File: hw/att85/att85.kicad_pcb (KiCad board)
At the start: 4 copper layers, 80 x 40 mm, 45 parts, among them J101 Barrel_Jack_Switch, J102 Screw_Terminal_01x03, J201 Conn_01x06, Q101 BC817, SW401 SW_Push, SW402 SW_Push, SW403 SW_Push, SW404 SW_Push, SW405 SW_Push, SW406 SW_Push, U201 STM32G030K8Tx, U202 74AHCT125, U301 VS1838B, U401 4050, U501 AMS1117-3.3

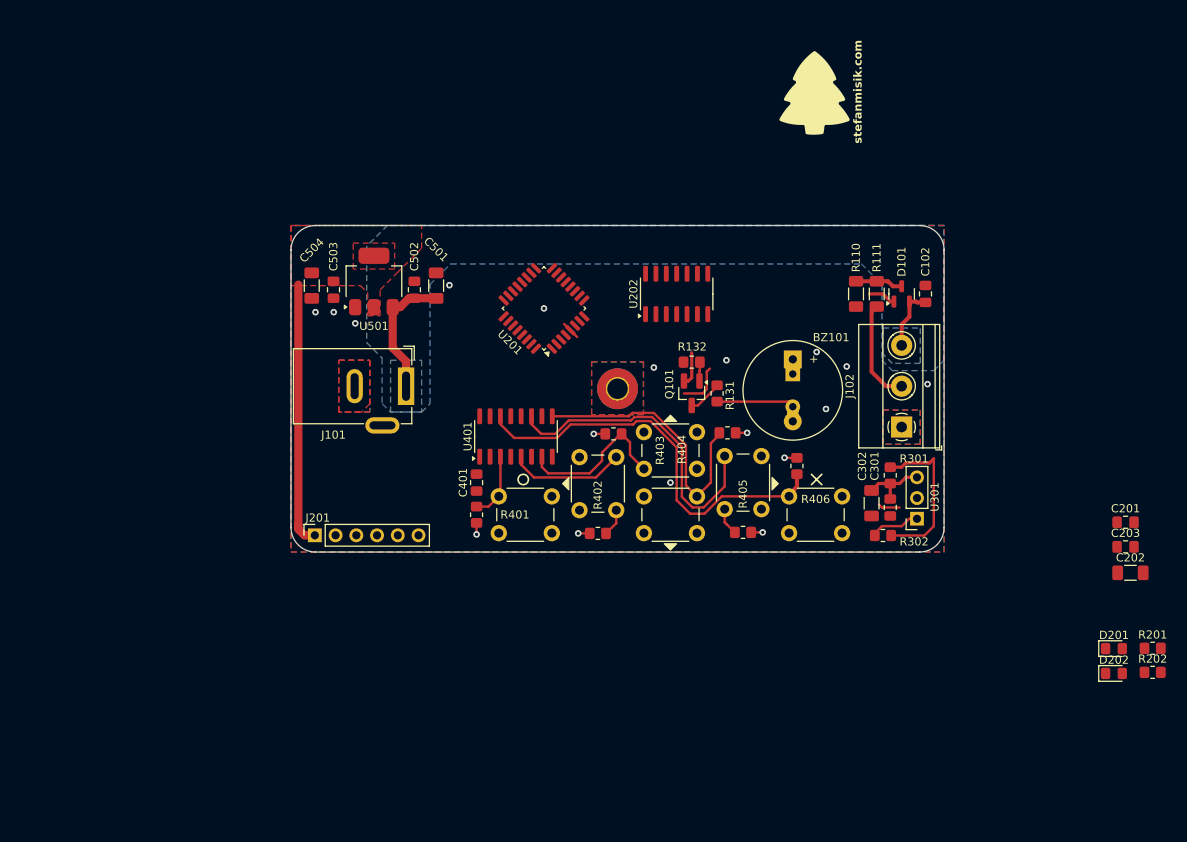
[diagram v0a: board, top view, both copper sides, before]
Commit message: chore(hw): add peripheral connections, layout power supply
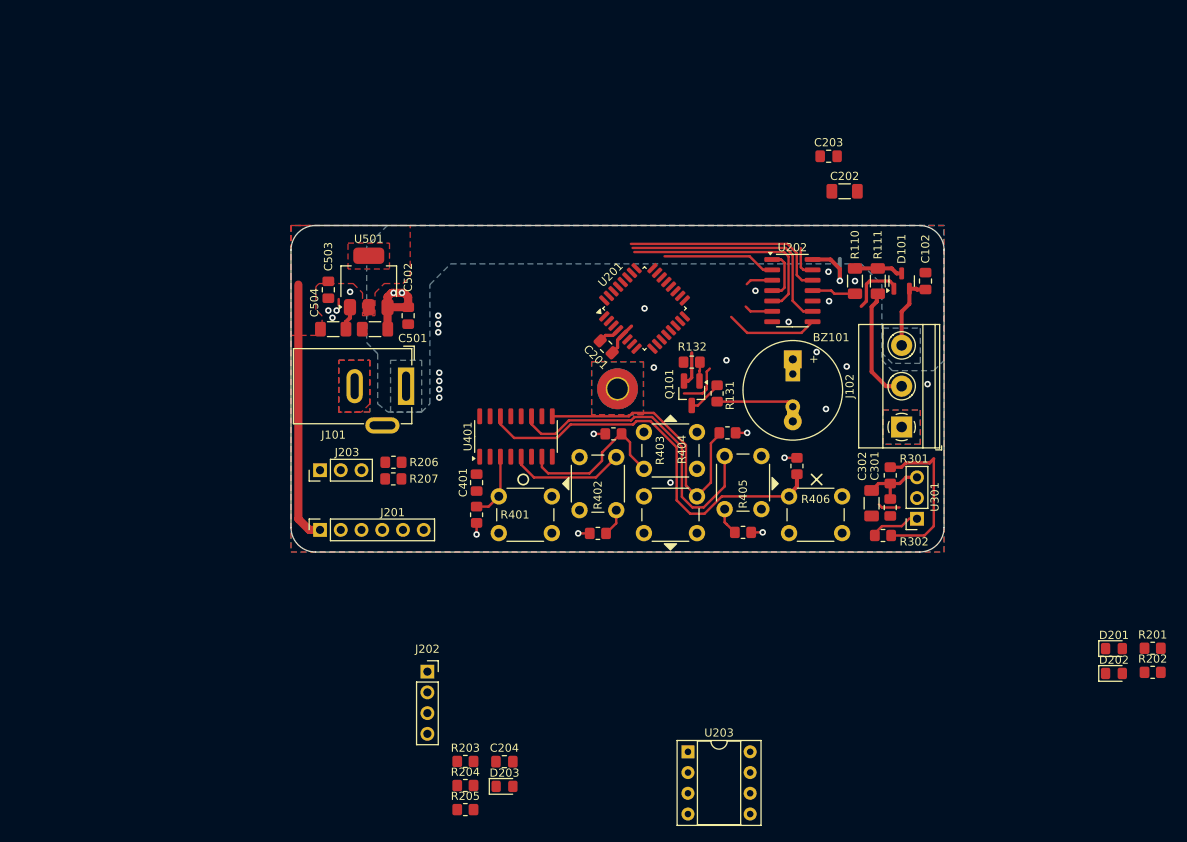
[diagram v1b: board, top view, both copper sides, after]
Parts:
- added C204: 100n, Capacitor_SMD:C_0805_2012Metric_Pad1.18x1.45mm_HandSolder, F.Cu at (145.5, 140.6)
- added D203: LED, LED_SMD:LED_0805_2012Metric_Pad1.15x1.40mm_HandSolder, F.Cu at (145.5, 143.6)
- added J202: Conn_01x04, Connector_PinSocket_2.54mm:PinSocket_1x04_P2.54mm_Vertical, F.Cu at (136.1, 129.6)
- added J203: Conn_01x03, Connector_PinHeader_2.54mm:PinHeader_1x03_P2.54mm_Vertical, F.Cu at (122.9, 104.9)
- added R203: 1K, Resistor_SMD:R_0805_2012Metric_Pad1.20x1.40mm_HandSolder, F.Cu at (140.7, 140.6)
- added R204: 10K, Resistor_SMD:R_0805_2012Metric_Pad1.20x1.40mm_HandSolder, F.Cu at (140.7, 143.5)
- added R205: 10K, Resistor_SMD:R_0805_2012Metric_Pad1.20x1.40mm_HandSolder, F.Cu at (140.7, 146.5)
- added R206: 33R, Resistor_SMD:R_0805_2012Metric_Pad1.20x1.40mm_HandSolder, F.Cu at (131.9, 103.9)
- added R207: 33R, Resistor_SMD:R_0805_2012Metric_Pad1.20x1.40mm_HandSolder, F.Cu at (131.9, 106.0)
- added U203: CAT24C256, Package_DIP:DIP-8_W7.62mm_Socket, F.Cu at (168.0, 139.4)
- moved C201 67.2 mm to (158.0, 89.8), turned to -45 degrees
- moved C203 60.1 mm to (185.2, 66.4)
- moved C202 58.4 mm to (187.2, 70.7)
- moved U202 14.2 mm to (180.8, 82.9), turned to 0 degrees
- moved U201 12.3 mm to (162.7, 85.1), turned to 45 degrees
- moved C501 9.20 mm to (129.7, 87.6), turned to 180 degrees
- moved C504 5.95 mm to (124.5, 87.6), turned to 0 degrees
- moved C502 3.27 mm to (133.7, 86.0), turned to -90 degrees
- moved R110 1.58 mm to (188.5, 81.7)
- moved R111 1.58 mm to (191.3, 81.7)
- moved C102 1.57 mm to (197.1, 81.7)
- moved D101 1.57 mm to (194.2, 81.7)
- moved J201 0.92 mm to (122.9, 112.2)
- moved C503 0.64 mm to (124.0, 82.8)
- moved U501 0.63 mm to (128.9, 81.8)
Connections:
- U201 pad 1: unconnected-(U201-PB9-Pad1) -> /CPU/I2C_SDA
- U201 pad 10: unconnected-(U201-PA3-Pad10) -> /CPU/DEBUG_RX
- U201 pad 16: unconnected-(U201-PB1-Pad16) -> /CPU/STATUS_LED1
- U201 pad 17: unconnected-(U201-PB2-Pad17) -> /CPU/STATUS_LED2
- U201 pad 18: unconnected-(U201-PA8-Pad18) -> /CPU/STATUS_LED3
- U201 pad 32: unconnected-(U201-PB8-Pad32) -> /CPU/I2C_SCL
- U201 pad 9: unconnected-(U201-PA2-Pad9) -> /CPU/DEBUG_TX
- U202 pad 11: unconnected-(U202-Pad11) -> /CPU/LED_DATA
- U202 pad 12: GND -> /CPU/LED_DATA_3V3
- U202 pad 2: /CPU/LED_DATA_3V3 -> /CPU/STATUS_LED1
- U202 pad 3: /CPU/LED_DATA -> Net-(D201-A)
- U202 pad 5: /CPU/STATUS_LED_G -> /CPU/STATUS_LED2
- U202 pad 6: Net-(D201-A) -> Net-(D202-A)
- U202 pad 8: Net-(D202-A) -> Net-(D203-A)
- U202 pad 9: /CPU/STATUS_LED_R -> /CPU/STATUS_LED3
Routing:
- net /CPU/STATUS_LED3: track 0.00 -> 28.6 mm
- net /CPU/STATUS_LED2: track 0.00 -> 26.1 mm
- net /CPU/LED_DATA_3V3: track 0.00 -> 25.7 mm
- net GND: track 18.2 -> 38.0 mm, vias 12 -> 24
- net /CPU/STATUS_LED1: track 0.00 -> 13.9 mm
- net Net-(D203-A): track 0.00 -> 11.3 mm
- net /CPU/LED_DATA: track 0.00 -> 5.48 mm
- net +5V: track 102.3 -> 106.4 mm, vias 6 -> 9
- net Net-(D202-A): track 0.00 -> 3.48 mm
- net Net-(D201-A): track 0.00 -> 3.31 mm
- net +3.3V: track 52.0 -> 54.4 mm
- net Net-(J102-Pin_2): track 12.7 -> 14.2 mm

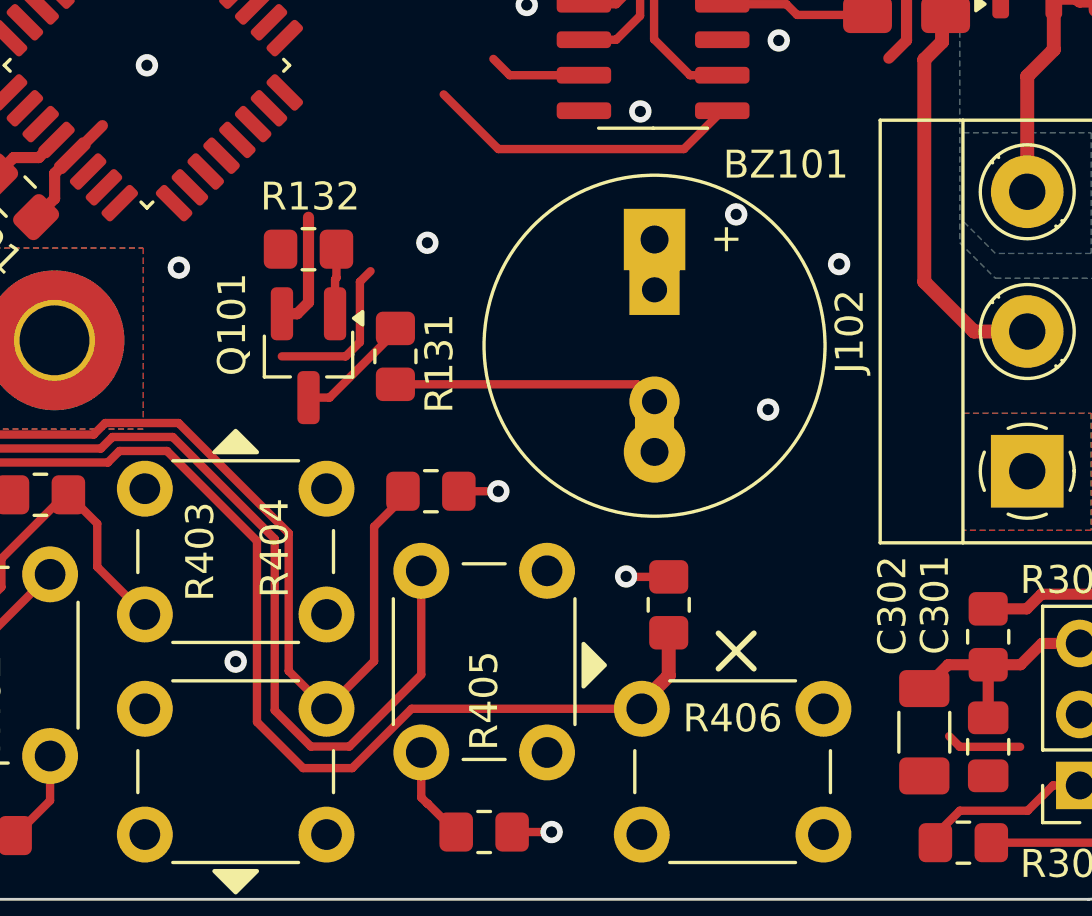
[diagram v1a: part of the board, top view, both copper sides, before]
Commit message: chore(hw): move buzzer driving circuitry
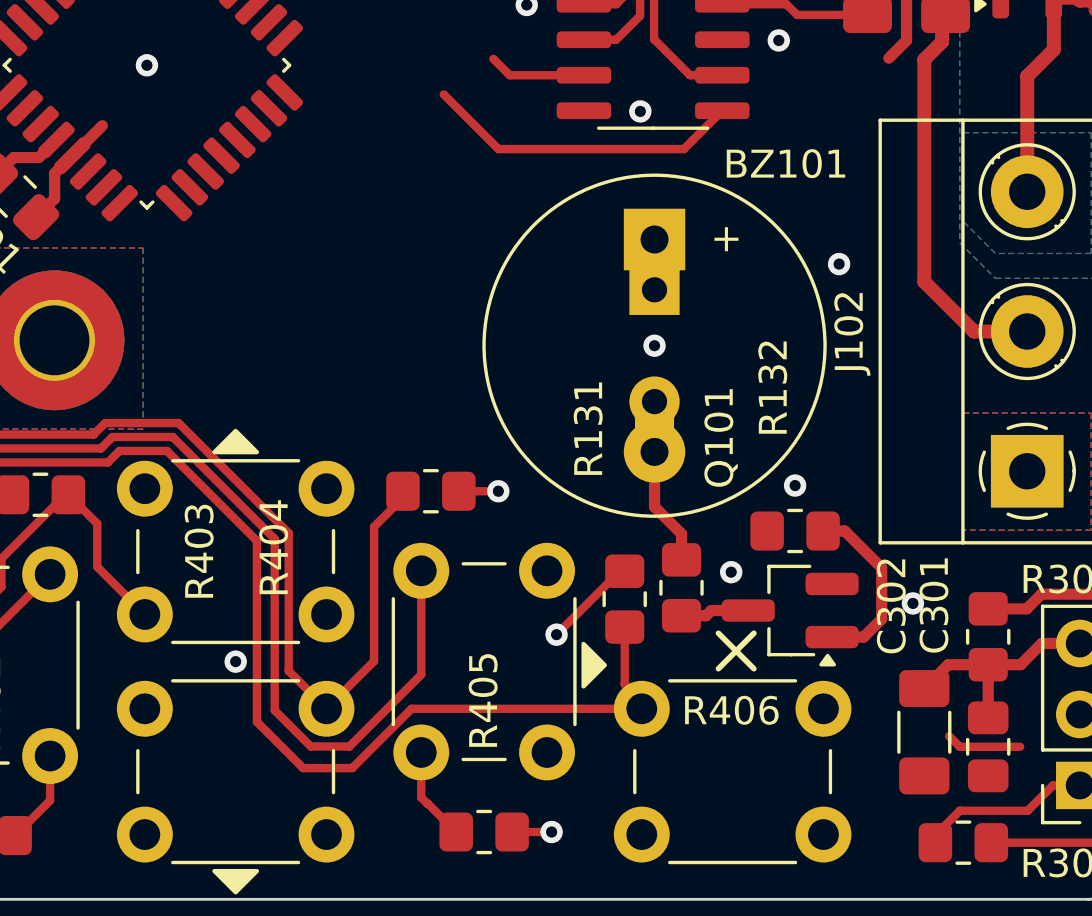
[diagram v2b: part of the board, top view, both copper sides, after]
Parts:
- moved R132 20.1 mm to (185.9, 101.8)
- moved Q101 19.5 mm to (185.7, 104.6), turned to 180 degrees
- moved R131 13.2 mm to (181.8, 103.8), turned to -90 degrees
- moved R406 1.59 mm to (179.8, 104.2)
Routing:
- net GND: track 38.0 -> 28.1 mm
- net Net-(BZ101--): track 9.53 -> 4.26 mm
- net Net-(Q101-B): track 2.33 -> 6.52 mm
- net +5V: track 106.4 -> 104.5 mm
- net Net-(Q101-C): track 4.20 -> 2.47 mm

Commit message: chore(hw): prepare layout
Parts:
- moved J202 93.3 mm to (215.3, 80.3), turned to 90 degrees
- moved U203 86.4 mm to (87.1, 109.0)
- moved C202 13.4 mm to (185.9, 84.1), turned to -90 degrees
- moved C203 13.1 mm to (185.8, 79.5), turned to 90 degrees
- moved U201 10.4 mm to (152.3, 85.0)
- moved C201 10.4 mm to (147.6, 89.7)
- moved C102 3.30 mm to (196.0, 84.8), turned to 180 degrees
- moved C401 2.62 mm to (144.5, 105.4), turned to 0 degrees
- moved J201 2.11 mm to (122.9, 110.1)
- moved R402 1.78 mm to (158.8, 112.5)
- moved R405 1.78 mm to (173.0, 112.5)
- moved D101 1.65 mm to (195.8, 81.7)
- moved R110 1.65 mm to (190.1, 81.7)
- moved R111 1.65 mm to (192.9, 81.7)
- moved U401 0.66 mm to (147.6, 100.6)
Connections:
- U401 pad 10: /CPU/BTN_DOWN -> /CPU/BTN_UP
- U401 pad 11: Net-(R405-Pad1) -> Net-(R406-Pad1)
- U401 pad 12: /CPU/BTN_RIGHT -> /CPU/BTN_X
- U401 pad 14: Net-(R406-Pad1) -> Net-(R405-Pad1)
- U401 pad 15: /CPU/BTN_X -> /CPU/BTN_RIGHT
- U401 pad 6: /CPU/BTN_UP -> /CPU/BTN_DOWN
- U401 pad 7: Net-(R403-Pad1) -> Net-(R404-Pad1)
- U401 pad 9: Net-(R404-Pad1) -> Net-(R403-Pad1)
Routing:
- net +3.3V: track 54.4 -> 139.8 mm, vias 0 -> 2
- net GND: track 28.1 -> 100.9 mm, vias 24 -> 26
- net +5V: track 104.5 -> 151.4 mm
- net /CPU/IR_DATA_3V3: track 6.17 -> 32.4 mm
- net /CPU/BTN_DOWN: track 0.00 -> 13.2 mm
- net /CPU/BTN_LEFT: track 0.00 -> 11.2 mm
- net Net-(R404-Pad1): track 40.4 -> 29.9 mm
- net /CPU/BUZZER_3V3: track 0.00 -> 10.1 mm
- net /CPU/BTN_O: track 0.00 -> 9.41 mm
- net Net-(R406-Pad1): track 56.9 -> 48.8 mm
- net Net-(R405-Pad1): track 48.8 -> 43.5 mm
- net Net-(R403-Pad1): track 25.9 -> 21.5 mm
- net /CPU/BTN_X: track 0.00 -> 2.60 mm
- net /CPU/BTN_RIGHT: track 0.00 -> 2.48 mm
- net /CPU/BTN_UP: track 0.00 -> 2.35 mm
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
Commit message: chore(hw): add buzzer connection
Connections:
- U201 pad 13: unconnected-(U201-PA6-Pad13) -> /CPU/BUZZER_3V3

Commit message: chore(hw): partial layout
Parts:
- moved U203 125.9 mm to (213.0, 104.9)
- moved R202 72.6 mm to (168.9, 83.4), turned to 180 degrees
- moved R201 72.1 mm to (168.9, 81.3), turned to 180 degrees
- moved D202 66.4 mm to (172.7, 83.4)
- moved D201 65.7 mm to (172.7, 81.3)
- moved D203 64.1 mm to (172.7, 85.6)
- moved R203 61.8 mm to (168.9, 85.6), turned to 180 degrees
- moved C201 16.7 mm to (164.2, 90.9), turned to 90 degrees
- moved U201 7.12 mm to (159.4, 85.2), turned to 90 degrees
- moved R207 3.10 mm to (132.0, 102.9)
- moved R132 1.76 mm to (187.2, 100.6), turned to -90 degrees
- moved R206 0.97 mm to (132.0, 104.9)
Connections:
- U201 pad 26: unconnected-(U201-PA15-Pad26) -> /CPU/BTN_O
- U201 pad 27: unconnected-(U201-PB3-Pad27) -> /CPU/BTN_LEFT
- U201 pad 28: unconnected-(U201-PB4-Pad28) -> /CPU/BTN_DOWN
- U201 pad 29: unconnected-(U201-PB5-Pad29) -> /CPU/BTN_RIGHT
- U201 pad 30: unconnected-(U201-PB6-Pad30) -> /CPU/BTN_X
- U201 pad 31: unconnected-(U201-PB7-Pad31) -> /CPU/BTN_UP
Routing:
- net GND: track 100.9 -> 227.7 mm, vias 26 -> 34
- net /CPU/SWDIO: track 0.00 -> 55.8 mm, vias 0 -> 1
- net /CPU/DEBUG_TX: track 0.00 -> 55.6 mm, vias 0 -> 2
- net /CPU/DEBUG_RX: track 0.00 -> 54.5 mm, vias 0 -> 2
- net /CPU/SWCLK: track 0.00 -> 53.9 mm, vias 0 -> 1
- net /CPU/~{RESET}: track 0.00 -> 51.4 mm, vias 0 -> 1
- net +3.3V: track 139.8 -> 178.9 mm, vias 2 -> 4
- net /CPU/IR_DATA_3V3: track 32.4 -> 66.7 mm, vias 0 -> 2
- net /CPU/BUZZER_3V3: track 10.1 -> 35.4 mm
- net /CPU/BTN_O: track 9.41 -> 32.5 mm
- net /CPU/BTN_LEFT: track 11.2 -> 33.2 mm
- net /CPU/BTN_DOWN: track 13.2 -> 34.3 mm
- net /CPU/BTN_RIGHT: track 2.48 -> 20.6 mm
- net /CPU/BTN_X: track 2.60 -> 16.8 mm
- net +5V: track 151.4 -> 163.6 mm
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
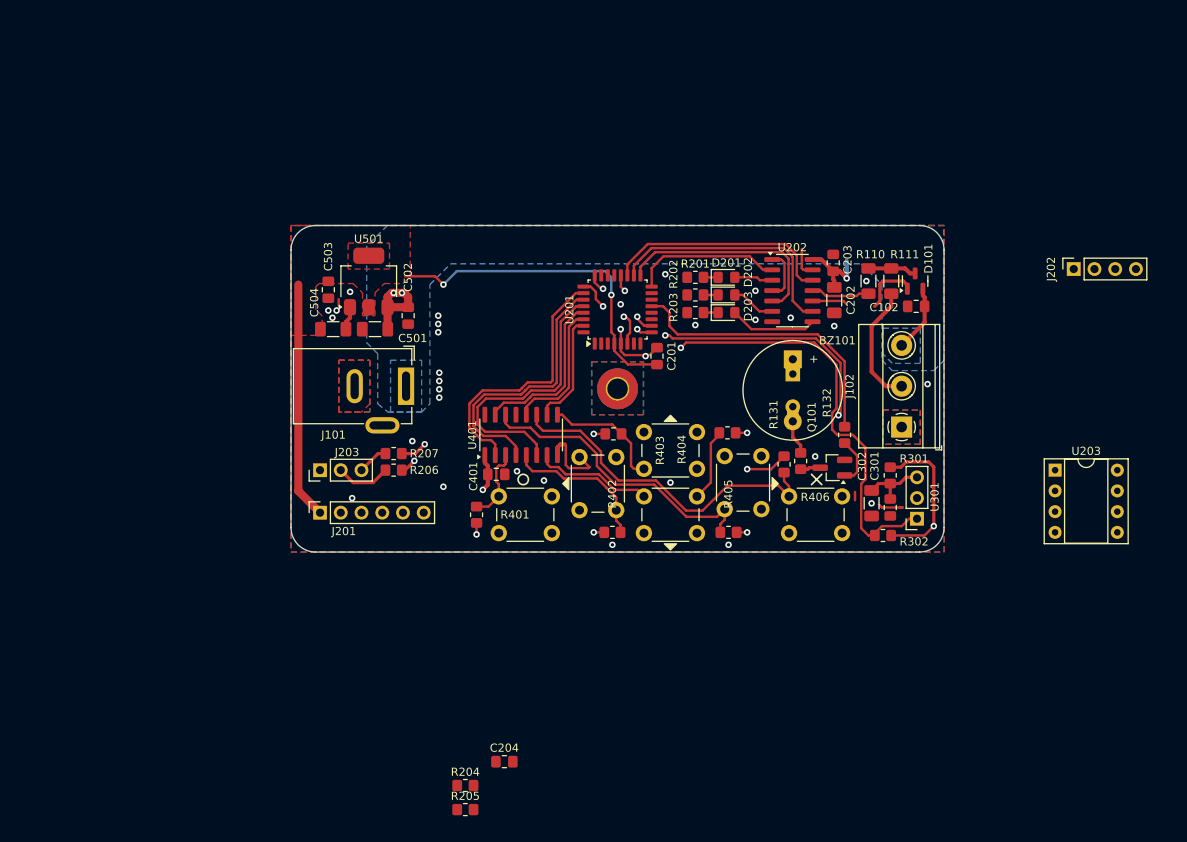
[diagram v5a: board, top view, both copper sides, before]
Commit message: chore(hw): move debug UART header
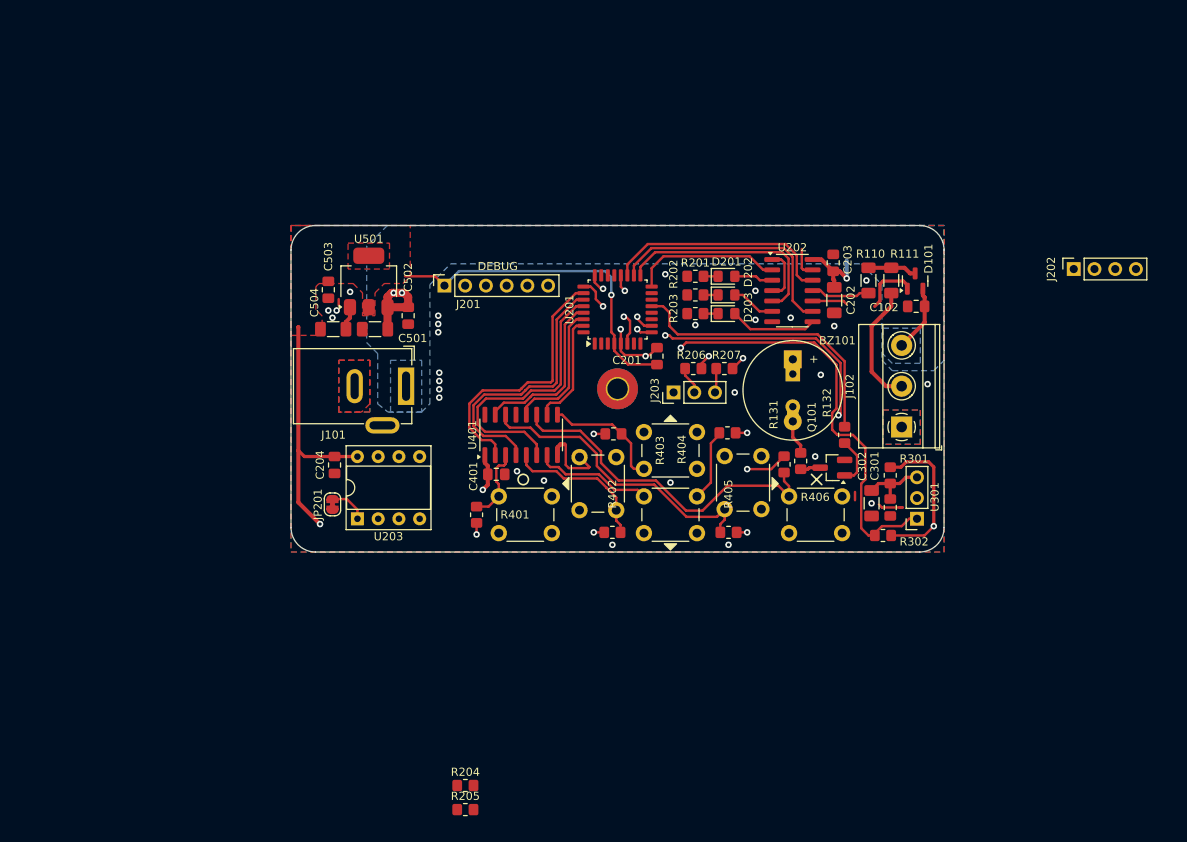
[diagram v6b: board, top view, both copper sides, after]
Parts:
- added JP201: Jumper_2_Bridged, Jumper:SolderJumper-2_P1.3mm_Bridged_RoundedPad1.0x1.5mm, F.Cu at (124.5, 109.1)
- moved U203 85.7 mm to (127.5, 110.9), turned to 90 degrees
- moved J203 44.3 mm to (166.2, 95.4)
- moved C204 41.9 mm to (124.7, 104.3), turned to -90 degrees
- moved R207 41.8 mm to (172.5, 92.5)
- moved R206 38.8 mm to (168.7, 92.5)
- moved J201 31.7 mm to (138.2, 82.3)
- moved D201 0.13 mm to (172.7, 81.2)
- moved D203 0.13 mm to (172.7, 85.7)
- moved R201 0.13 mm to (168.9, 81.2)
- moved R203 0.13 mm to (168.9, 85.7)
- moved R110 0.08 mm to (190.1, 81.7)
- moved R111 0.08 mm to (192.9, 81.7)
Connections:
- U203 pad 1: GND -> Net-(JP201-B)
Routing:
- net GND: track 227.7 -> 115.4 mm, vias 34 -> 32
- net /CPU/DEBUG_TX: track 55.6 -> 14.4 mm
- net /CPU/DEBUG_RX: track 54.5 -> 19.2 mm
- net /CPU/SWDIO: track 55.8 -> 20.8 mm
- net /CPU/~{RESET}: track 51.4 -> 17.3 mm
- net /CPU/SWCLK: track 53.9 -> 20.4 mm
- net Net-(JP201-B): track 0.00 -> 4.72 mm
- net Net-(J203-Pin_2): track 6.74 -> 3.39 mm
- net +3.3V: track 178.9 -> 181.3 mm
- net Net-(J203-Pin_3): track 3.78 -> 2.98 mm
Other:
- board text added: "DEBUG"

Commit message: chore(hw): almost final layout
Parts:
- removed JP201: Jumper_2_Bridged, Jumper:SolderJumper-2_P1.3mm_Bridged_RoundedPad1.0x1.5mm
- moved J202 74.9 mm to (140.7, 87.2)
- moved R205 42.9 mm to (138.0, 103.6), turned to -90 degrees
- moved R204 36.2 mm to (138.0, 107.4), turned to 90 degrees
- moved C201 4.83 mm to (159.4, 90.8), turned to 0 degrees
- moved U201 0.76 mm to (159.4, 84.5)
- moved R131 0.36 mm to (181.8, 104.1)
- moved C204 0.25 mm to (124.5, 104.3)
- moved R406 0.05 mm to (179.8, 104.1)
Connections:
- J201 pad 1: +3.3V -> /CPU/SWCLK
- J201 pad 2: /CPU/SWDIO -> GND
- J201 pad 3: /CPU/SWCLK -> /CPU/SWDIO
- J201 pad 4: GND -> +3.3V
- U203 pad 1: Net-(JP201-B) -> GND
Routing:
- net /CPU/I2C_SCL: track 0.00 -> 59.3 mm, vias 0 -> 1
- net /CPU/I2C_SDA: track 0.00 -> 50.3 mm, vias 0 -> 1
- net +3.3V: track 181.3 -> 205.5 mm, vias 4 -> 5
- net GND: track 115.4 -> 130.1 mm, vias 32 -> 35
- net /CPU/SWCLK: track 20.4 -> 31.0 mm
- net /CPU/SWDIO: track 20.8 -> 30.7 mm
- net Net-(JP201-B): track 4.72 -> 0.00 mm
- net /CPU/BTN_O: track 32.5 -> 31.4 mm
- net /CPU/BTN_DOWN: track 34.3 -> 33.2 mm
- net /CPU/BTN_LEFT: track 33.2 -> 32.3 mm
- net /CPU/BTN_X: track 16.8 -> 15.9 mm
- net /CPU/IR_DATA_3V3: track 66.7 -> 65.9 mm
- net /CPU/BTN_RIGHT: track 20.6 -> 20.1 mm
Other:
- board text added: "DISPLAY"
- board text added: "EEPROM"
- board text added: "G"
- board text added: "R"
- board text added: "UART"
- board text added: "Y"
